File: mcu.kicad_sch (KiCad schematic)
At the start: 35 parts, among them Q1 2N7002, Q2 2N7002, Q3 2N7002, Q4 2N7002, Q6 2N7002, Q8 2N7002, Q9 2N7002, U11 NUCLEOH723ZG

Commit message: Place all componenets
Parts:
- removed R65: 33R, Resistor_SMD:R_0805_2012Metric, symbol Device:R
- removed U11: NUCLEOH723ZG, NUCLEOH723ZG:MODULE_NUCLEOH723ZG, symbol NUCLEOH723ZG:NUCLEOH723ZG
- added U11: NUCLEOH723ZG, NUCLEO232ZG:MODULE_NUCLEOH723ZG, symbol NUCLEO232ZG:NUCLEOH723ZG
- renumbered Q6 to Q5, Q8 to Q6, Q9 to Q7, R72 to R67, R73 to R68, R75 to R69, R76 to R70, R74 to R71, R77 to R72, R78 to R73, R79 to R74, R93 to R75, R96 to R76, R116 to R77, R117 to R78, R56 to R79, R134 to R80, R149 to R81, R152 to R82, R153 to R83, R154 to R84, R155 to R85
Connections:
- net AC_DC_CH1_MCU: now also U11.CN7_19 (D25/SPI_B_MISO)
- net AC_DC_CH2_MCU: now also U11.CN7_11 (D21/I2S_B_MCK)
- net CH1_ATTEN_MCU: now also U11.CN9_26 (D62/SAI_B_MCLK)
- net CH2_ATTEN_MCU: now also U11.CN7_15 (D23/I2S_B_CK/SPI_B_SCK)
- net DAC_ALM: now also U11.CN9_17 (D70/I2C_B_SMBA)
- net DAC_CLR: now also U11.CN9_28 (D63/SAI_B_FS)
- net DAC_RST: now also U11.CN9_24 (D61/SAI_B_SCK)
- net DAC_TEMP: now also U11.CN9_1 (A0/ADC12_INP15)
- net GND: now also U11.CN10_17 (GND_CN10), U11.CN10_22 (GND_CN10), U11.CN10_27 (GND_CN10), U11.CN10_3 (AGND_CN10), U11.CN10_5 (GND_CN10), U11.CN7_8 (GND_CN7), U11.CN8_11 (GND_CN8), U11.CN8_13 (GND_CN8), U11.CN9_12 (GND_CN9), U11.CN9_23 (GND_CN9)
- net GPIO_0: now also U11.CN10_8 (D4/IO)
- net GPIO_1: now also U11.CN10_31 (D33/TIMER_D_PWM1)
- net GPIO_2: now also U11.CN10_34 (D35/TIMER_C_PWM3)
- net GPIO_3: now also U11.CN10_32 (D36/TIMER_C_PWM2)
- net GPIO_4: now also U11.CN10_29 (D32/TIMER_C_PWM1)
- net GPIO_PD0: now also U11.CN9_19 (D69/I2C_B_SCL)
- net GPIO_PD1: now also U11.CN9_21 (D68/I2C_B_SDA)
- net GPIO_PD15: now also U11.CN7_18 (D9/TIMER_B_PWM2)
- net GPIO_PD2: now also U11.CN8_12 (D48/SDMMC_CMD)
- net GPIO_PD3: now also U11.CN9_10 (D55/USART_B_CTS)
- net GPIO_PD4: now also U11.CN9_8 (D54/USART_B_RTS)
- net GPIO_PD5: now also U11.CN9_6 (D53/USART_B_TX)
- net GPIO_PD6: now also U11.CN9_4 (D52/USART_B_RX)
- net GPIO_PD7: now also U11.CN9_2 (D51/USART_B_SCLK)
- net GPIO_PE0: now also U11.CN10_33 (D34/TIMER_B_ETR)
- net GPIO_PE10: now also U11.CN10_24 (D40/TIMER_A_PWM2N)
- net GPIO_PE11: now also U11.CN10_6 (D5/TIMER_A_PWM2)
- net GPIO_PE12: now also U11.CN10_26 (D39/TIMER_A_PWM3N)
- net GPIO_PE13: now also U11.CN10_10 (D3/TIMER_A_PWM3)
- net GPIO_PE15: now also U11.CN10_30 (D37/TIMER_A_BKIN1)
- net GPIO_PE4: now also U11.CN9_16 (D57/SAI_A_FS)
- net GPIO_PE5: now also U11.CN9_18 (D58/SAI_A_SCK)
- net GPIO_PE6: now also U11.CN9_20 (D59/SAI_A_SD)
- net GPIO_PE7: now also U11.CN10_20 (D41/TIMER_A_ETR)
- net GPIO_PE8: now also U11.CN10_18 (D42/TIMER_A_PWM1N)
- net GPIO_PE9: now also U11.CN10_4 (D6/TIMER_A_PWM1)
- net QSPI_CLK: now also U11.CN10_15 (D27/QSPI_CLK)
- net QSPI_CS: now also U11.CN10_13 (D26/QSPI_CS)
- net QSPI_IO0/GPIO_PD11: now also U11.CN10_23 (D30/QSPI_BK1_IO0)
- net QSPI_IO1/GPIO_PD12: now also U11.CN10_21 (D29/QSPI_BK1_IO1)
- net QSPI_IO2/GPIO_PE2: now also U11.CN10_25 (D31/QSPI_BK1_IO2)
- net QSPI_IO3/GPIO_PD13: now also U11.CN10_19 (D28/QSPI_BK1_IO3)
- net SPI_1_CS: now also U11.CN7_16 (D10/SPI_A_CS/TIM_B_PWM3)
- net SPI_1_MISO: now also U11.CN7_12 (D12/SPI_A_MISO)
- net SPI_1_MOSI: now also U11.CN7_14 (D11/SPI_A_MOSI/TIM_E_PWM1)
- net SPI_1_SCK: now also U11.CN7_10 (D13/SPI_A_SCK)
- net TRIGGER_AC_DC_MCU: now also U11.CN9_13 (D72/COMP1_INP)
- net TRIGG_1_MCU: now also U11.CN9_30 (D64/IO)
- net TRIGG_2_MCU: now also U11.CN9_29 (D65/IO)
- net USART_1_RX: now also U11.CN10_16 (D0/USART_A_RX)
- net USART_1_TX: now also U11.CN10_14 (D1/USART_A_TX)
- net at R70.1: now also U11.CN8_9 (5V_CN8)
- net at R69.1: now also U11.CN8_15 (VIN_CN8)
- new net GND_CN15: U11.CN15_1 (GND_CN15), U11.CN15_2 (GND_CN15)
- new net GND_CN16: U11.CN16_1 (GND_CN16), U11.CN16_2 (GND_CN16)
- new net GND_CN3: U11.CN3_1 (GND_CN3), U11.CN3_2 (GND_CN3)
- new net GND_CN4: U11.CN4_1 (GND_CN4), U11.CN4_2 (GND_CN4)
- no-connect marks 40 -> 42
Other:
- note removed: "Unused"

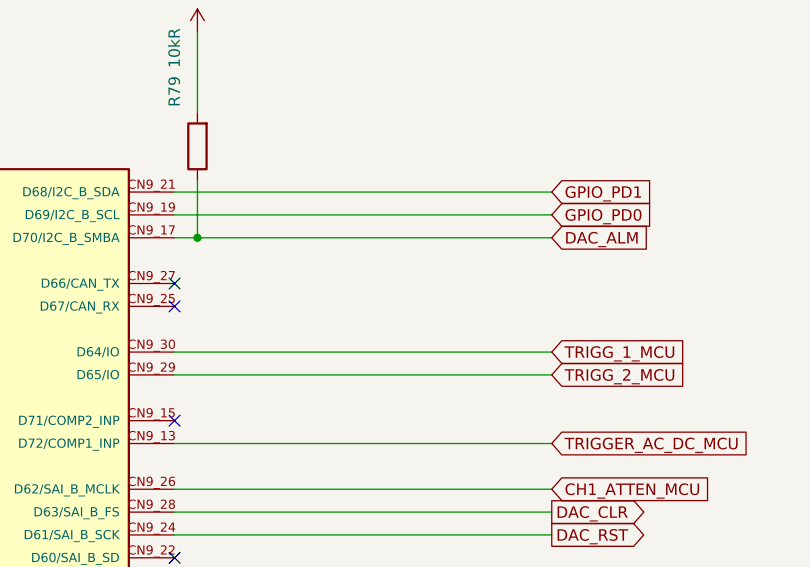
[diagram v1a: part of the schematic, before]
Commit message: Everything is routed
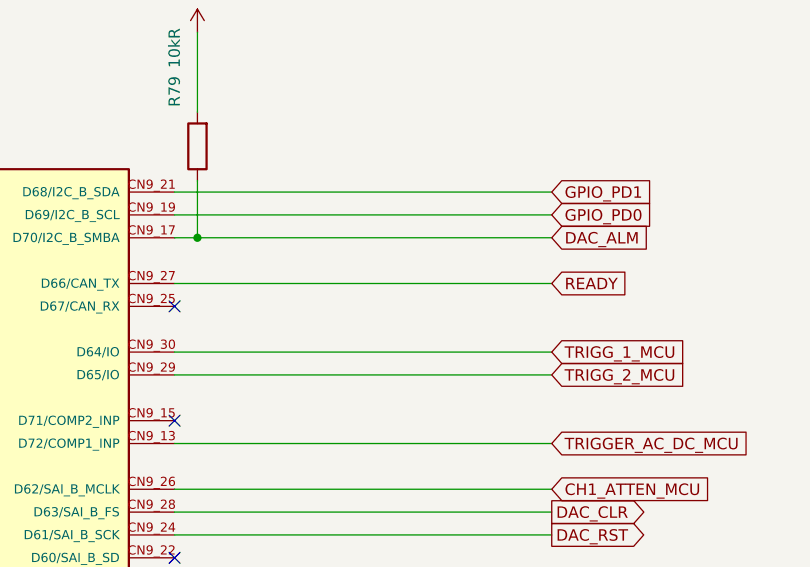
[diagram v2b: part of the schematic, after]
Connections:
- net READY: now reaches U11.CN9_27 (D66/CAN_TX)
- no-connect marks 42 -> 41
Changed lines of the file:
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@@
-	)
-	(no_connect
-		(at 308.61 128.27)
 	)
 	(no_connect
@@
 		(pts
 			(xy 173.99 121.92) (xy 173.99 125.73)
+		)
+		(stroke
+			(width 0)
+			(type default)
+		)
+	)
+	(wire
+		(pts
+			(xy 350.52 128.27) (xy 308.61 128.27)
 		)
 		(stroke
@@
 			(effects
 				(font
+					(size 1.27 1.27)
+				)
+				(justify left)
+				(hide yes)
+			)
+		)
+	)
+	(global_label "READY"
+		(shape input)
+		(at 350.52 128.27 0)
+		(fields_autoplaced yes)
+		(effects
+			(font
+				(size 1.27 1.27)
+			)
+			(justify left)
+		)
+		(property "Intersheetrefs" "${INTERSHEET_REFS}"
+			(at 359.3714 128.27 0)
+			(effects
+				(font

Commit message: Place most of the components in cart
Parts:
- removed unit 1 of U11

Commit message: Finish channel 1 rework
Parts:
- removed D5: 1N4148W, Diode_SMD:D_SOD-123, symbol Diode:1N4148W
- removed Q3: 2N7002, Package_TO_SOT_SMD:SOT-23, symbol Transistor_FET:2N7002
- removed R73: 220R, Resistor_SMD:R_0805_2012Metric, symbol Device:R
- removed R74: 10k, Resistor_SMD:R_0805_2012Metric, symbol Device:R
- renumbered D6 to D5, D7 to D6, D8 to D7, D9 to D8, Q4 to Q3, Q5 to Q4, Q6 to Q5, Q7 to Q6, R67 to R65, R68 to R66, R69 to R67, R70 to R68, R71 to R69, R72 to R70, R77 to R71, R78 to R72, R75 to R73, R76 to R74, R80 to R75, R81 to R76, R79 to R77, R82 to R78, R83 to R79, R84 to R80, R85 to R81
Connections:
- net TRIGGER_AC_DC_MCU: no longer names the net of U11.CN9_13 (D72/COMP1_INP)
- no-connect marks 41 -> 42
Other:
- moved on the sheet: D5, D6, D7, D8, Q3, Q4, Q5, Q6, R71, R72, R75, R76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

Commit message: Place all elements after rework
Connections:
- net GPIO_0 renamed GPIO_PE14
- net GPIO_1 renamed GPIO_PB0
- net GPIO_2 renamed GPIO_PB11
- net GPIO_3 renamed GPIO_PB10
- net GPIO_4 renamed GPIO_PA0
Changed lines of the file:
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@@
+	)
+	(no_connect
+		(at 308.61 158.75)
 	)
 	(no_connect
@@
 	(no_connect
 		(at 242.57 123.19)
-	)
-	(no_connect
-		(at 308.61 158.75)
 	)
 	(no_connect
@@
 		)
 	)
-	(global_label "GPIO_3"
+	(global_label "GPIO_PB10"
 		(shape input)
 		(at 350.52 190.5 0)
@@
 		)
 		(property "Intersheetrefs" "${INTERSHEET_REFS}"
-			(at 360.1576 190.5 0)
+			(at 363.9071 190.5 0)
 			(effects
 				(font
@@
 		)
 	)
-	(global_label "GPIO_0"
+	(global_label "GPIO_PE14"
 		(shape input)
 		(at 350.52 205.74 0)
@@
 		)
 		(property "Intersheetrefs" "${INTERSHEET_REFS}"
-			(at 360.1576 205.74 0)
+			(at 363.7861 205.74 0)
 			(effects
 				(font
@@
 		)
 	)
-	(global_label "GPIO_1"
+	(global_label "GPIO_PB0"
 		(shape input)
 		(at 350.52 198.12 0)
@@
 		)
 		(property "Intersheetrefs" "${INTERSHEET_REFS}"
-			(at 360.1576 198.12 0)
+			(at 362.6976 198.12 0)
 			(effects
 				(font
@@
 		)
 	)
-	(global_label "GPIO_4"
+	(global_label "GPIO_PA0"
 		(shape input)
 		(at 350.52 187.96 0)
@@
 		)
 		(property "Intersheetrefs" "${INTERSHEET_REFS}"
-			(at 360.1576 187.96 0)
+			(at 362.5162 187.96 0)
 			(effects
 				(font
@@
 		)
 	)
-	(global_label "GPIO_2"
+	(global_label "GPIO_PB11"
 		(shape input)
 		(at 350.52 193.04 0)
@@
 		)
 		(property "Intersheetrefs" "${INTERSHEET_REFS}"
-			(at 360.1576 193.04 0)
-			(effects
-				(font
+			(at 363.9071 193.04 0)
+			(effects
+				(font

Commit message: Finish release condidate 2
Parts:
- removed Q1, Q2, Q3, Q4, Q5, Q6: 2N7002, Package_TO_SOT_SMD:SOT-23, symbol Transistor_FET:2N7002
- added Q1, Q2, Q3, Q4, Q5, Q7: BC817, Package_TO_SOT_SMD:SOT-23, symbol Transistor_BJT:BC817
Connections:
- net AC_DC_CH1: now also Q4.3 (C)
- net AC_DC_CH2: now also Q5.3 (C)
- net CH1_ATTEN: now also Q2.3 (C)
- net CH2_ATTEN: now also Q3.3 (C)
- net GND: now also Q1.2 (E), Q2.2 (E), Q3.2 (E), Q4.2 (E), Q5.2 (E), Q7.2 (E)
- net TRIGG_1: now also Q7.3 (C)
- net TRIGG_2: now also Q1.3 (C)
- net at R78.1, R79.1: now also Q4.1 (B)
- net at R71.1, R72.1: now also Q2.1 (B)
- net at R75.1, R76.1: now also Q3.1 (B)
- net at R69.1, R70.1: now also Q1.1 (B)
- net at R65.1, R66.1: now also Q7.1 (B)
- net at R80.1, R81.1: now also Q5.1 (B)

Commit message: Trying to add symetry
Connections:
- net QSPI_CLK renamed QSPI_CLK/GPIO_PB2
- net QSPI_CS renamed QSPI_CS/GPIO_PG6

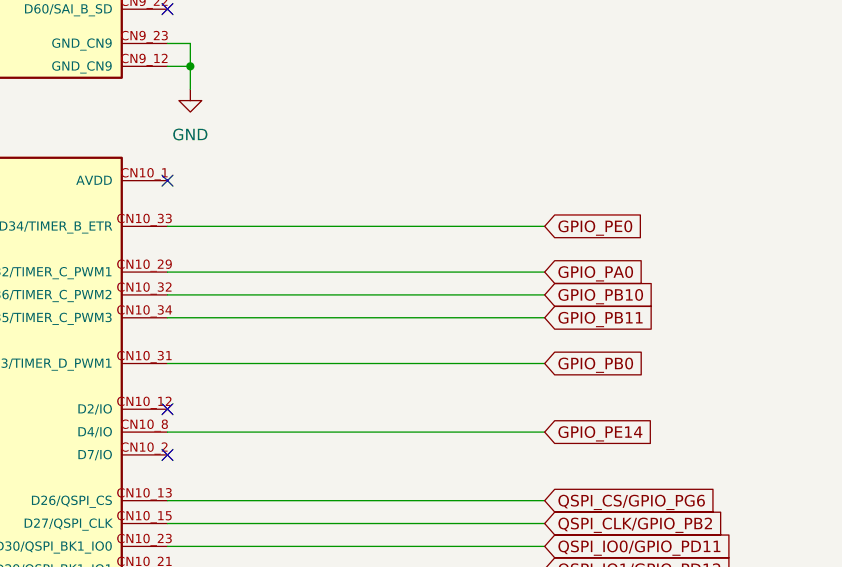
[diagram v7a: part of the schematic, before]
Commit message: Delete obsolete elements
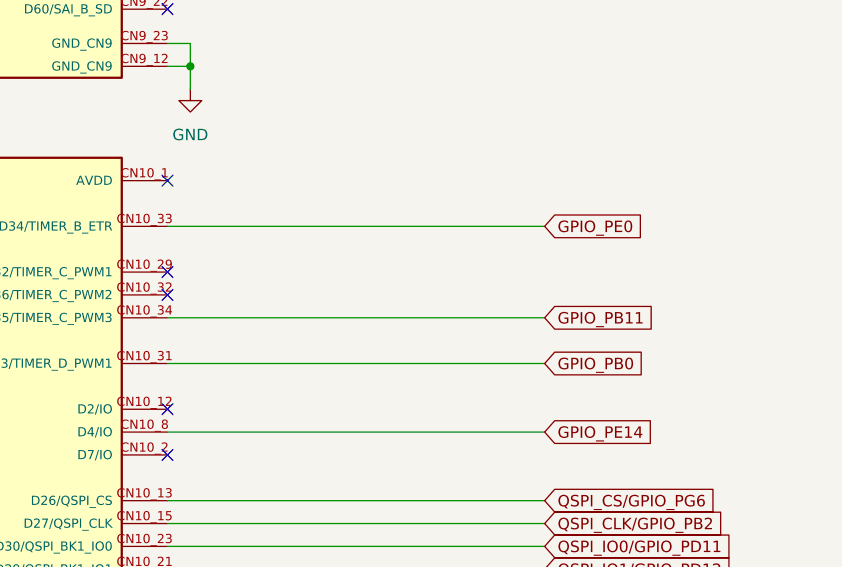
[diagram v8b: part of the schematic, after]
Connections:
- net GPIO_PA0: no longer names the net of U11.CN10_29 (D32/TIMER_C_PWM1)
- net GPIO_PB10: no longer names the net of U11.CN10_32 (D36/TIMER_C_PWM2)
- no-connect marks 42 -> 44
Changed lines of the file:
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@@
+	)
+	(no_connect
+		(at 308.61 190.5)
 	)
 	(no_connect
@@
 	)
 	(no_connect
+		(at 308.61 187.96)
+	)
+	(no_connect
 		(at 308.61 130.81)
 	)
@@
 	(wire
 		(pts
-			(xy 308.61 190.5) (xy 350.52 190.5)
-		)
-		(stroke
-			(width 0)
-			(type default)
-		)
-	)
-	(wire
-		(pts
 			(xy 290.83 308.61) (xy 290.83 311.15)
 		)
@@
 		(pts
 			(xy 115.57 321.31) (xy 115.57 318.77)
-		)
-		(stroke
-			(width 0)
-			(type default)
-		)
-	)
-	(wire
-		(pts
-			(xy 308.61 187.96) (xy 350.52 187.96)
 		)
 		(stroke
@@
 		)
 	)
-	(global_label "GPIO_PB10"
-		(shape input)
-		(at 350.52 190.5 0)
-		(fields_autoplaced yes)
-		(effects
-			(font
-				(size 1.27 1.27)
-			)
-			(justify left)
-		)
-		(property "Intersheetrefs" "${INTERSHEET_REFS}"
-			(at 363.9071 190.5 0)
-			(effects
-				(font
-					(size 1.27 1.27)
-				)
-				(justify left)
-				(hide yes)
-			)
-		)
-	)
 	(global_label "TRIGG_2_MCU"
 		(shape input)
@@
 				(hide yes)
 			)
-		)
-	)
-	(global_label "GPIO_PA0"
-		(shape input)
-		(at 350.52 187.96 0)
-		(fields_autoplaced yes)
-		(effects
-			(font
-				(size 1.27 1.27)
-			)
-			(justify left)
-		)
-		(property "Intersheetrefs" "${INTERSHEET_REFS}"
-			(at 362.5162 187.96 0)
-			(effects
-				(font
-					(size 1.27 1.27)
-				)
-				(justify left)
-				(hide yes)
-			)
